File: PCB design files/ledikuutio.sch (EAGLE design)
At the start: 54 parts, among them IC1 ATMEGA328P, IC3 74HC595D, Q2 MOSFET-NCHANNELSMD, Q3 16mhz, T1 TIP42, T2 TIP42, T3 TIP42, T4 TIP42, T5 TIP42, T6 TIP42, T7 TIP42, T8 TIP42, X1 2516-, X2 5566-20, X3 2516-, X4 2516-, X5 2516-, X6 2510-

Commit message: Updated the designs...
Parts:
- added C18, C19: 100nF, rcl:C-EUC0603
- added IC2: ISO7221A, texas:ISO7221A
- added R11, R12, R13, R14, R15, R16, R17, R18: 1k, rcl:R-EU_M0805
- F1, F2: value (none) -> 2A; device fuse:GSH15 -> special:FUSE
- R10, R3, R4, R5, R6, R7, R8, R9: device rc-master:R_0805 -> rcl:R-EU_M0805
- R2: device resistor:R-US_R0805 -> rcl:R-EU_M0805
- U$1, U$2, U$3, U$4: value TLC5940TLC5940NT -> TLC5940TLC5940PWP; device elovalo:TLC5940TLC5940NT -> elovalo:TLC5940TLC5940PWP
- UART: device con-lsta:FE06-1 -> elovalo:FE06-1
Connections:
- removed net DCPRG: IC1.PD6(AIN0), U$1TLC5940.DCPRG, U$2TLC5940.DCPRG, U$3TLC5940.DCPRG, U$4TLC5940.DCPRG
- removed net VPRG: IC1.PD5(T1), U$1TLC5940.VPRG, U$2TLC5940.VPRG, U$3TLC5940.VPRG, U$4TLC5940.VPRG
- new net GND1: C18.2, IC2.GND1, UART.1
- new net RXD_FT232R: IC2.INB, UART.5
- new net TXD_FT232R: IC2.OUTA, UART.4
- new net VDD: C18.1, IC2.VCC1, UART.3
- net +5V: now also F2.2, IC3A.SCL; no longer F1.1
- net BLANK: now also IC1.PB2(SS/OC1B); no longer IC1.PD7(AIN1)
- net GND: now also C19.2, IC2.GND2, U$1TLC5940.DCPRG, U$1TLC5940.VPRG, U$1TLC5940_PWR.GND@1, U$2TLC5940.DCPRG, U$2TLC5940.VPRG, U$2TLC5940_PWR.GND@1, U$3TLC5940.DCPRG, U$3TLC5940.VPRG, U$3TLC5940_PWR.GND@1, U$4TLC5940.DCPRG, U$4TLC5940.VPRG, U$4TLC5940_PWR.GND@1; no longer U$1TLC5940_PWR.GND, U$2TLC5940_PWR.GND, U$3TLC5940_PWR.GND, U$4TLC5940_PWR.GND, UART.1
- net N$10: now also R18.2
- net N$11: now also R12.2
- net N$12: now also R13.2
- net N$13: now also R15.2
- net N$14: now also R17.2
- net N$23: now also R13.1
- net N$24: now also R12.1
- net N$25: now also R11.1
- net N$26: now also R14.1
- net N$27: now also R15.1
- net N$28: now also R16.1
- net N$29: now also R17.1
- net N$30: now also R18.1
- net N$48: now also F2.1; no longer F1.2
- net N$5: now also F1.1; no longer F2.2
- net N$7: now also R11.2
- net N$8: now also R14.2
- net N$9: now also R16.2
- net PS_ON: now also IC1.PD3(INT1); no longer IC1.PD4(XCK/T0)
- net RXD: now also IC2.OUTB; no longer UART.4
- net TXD: now also IC2.INA; no longer UART.5
- net VCC: now also C19.1, F1.2, IC2.VCC2; no longer F2.1, IC3A.SCL, UART.3
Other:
- note added: "Kysy joelilta oikea pinijärjestys..."
- note removed: "Power supply"
- moved on the sheet: C1, C10, C11, C12, C13, C14, C15, C16, C17, C2, C3, C4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

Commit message: Signal area in PCB almost ready.
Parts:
- removed F1, F2: 2A, special:FUSE
- added C20, C22: 10nF, rcl:C-EUC0805
- added C21, C23: 100nF, rcl:C-EUC0805
- added R19, R20: 10k, rcl:R-EU_M0805
- added S1: RESET, SparkFun:SWITCH-MOMENTARY-2SMD
- added X7: ANALOG IO, con-3m:2510-
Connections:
- removed net N$48: C17.+, F2.1, X2-19.S, X2-20.S, X2-4.S, X2-6.S
- removed net N$5: F1.1, X2-9.S
- new net ADC0: IC1.PC0(ADC0), X7-1.KL
- new net ADC1: IC1.PC1(ADC1), X7-2.KL
- new net ADC2: IC1.PC2(ADC2), X7-3.KL
- new net ADC3: IC1.PC3(ADC3), X7-4.KL
- new net ADC4: IC1.PC4(ADC4/SDA), X7-5.KL
- new net ADC5: IC1.PC5(ADC5/SCL), X7-6.KL
- new net ADC6: IC1.ADC6, X7-7.KL
- new net ADC7: IC1.ADC7, X7-8.KL
- net +5V: now also C17.+, X2-19.S, X2-20.S, X2-4.S, X2-6.S; no longer F2.2
- net GND: now also C20.2, C21.2, C22.2, C23.2, IC1.AGND, R19.2, S1.2, X7-10.KL
- net PS_ON: now also R19.1
- net RESET: now also R20.1, S1.1
- net VCC: now also C20.1, C21.1, C22.1, C23.1, IC1.AVCC, R20.2, X2-9.S, X7-9.KL; no longer F1.2
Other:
- note added: "AVCC decoupling"
- moved on the sheet: C1, C2, Q3

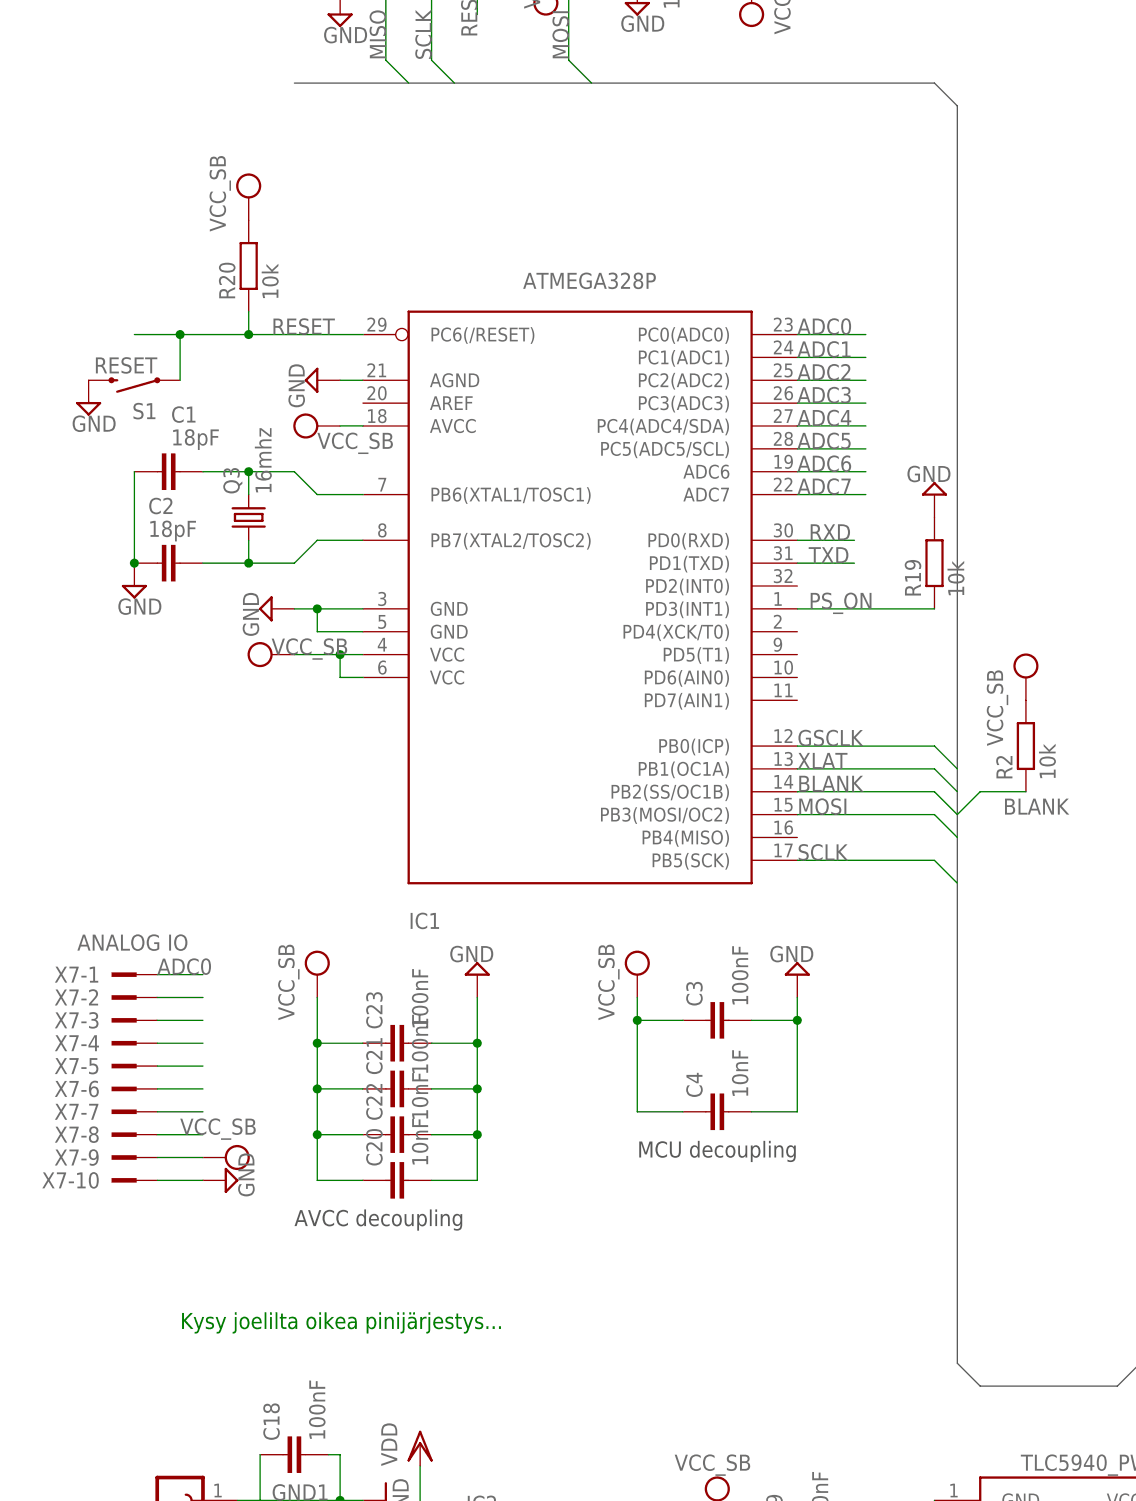
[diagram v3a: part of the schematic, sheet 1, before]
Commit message: Add up to date schematics.pdf and minor changes to the chematic and layout.
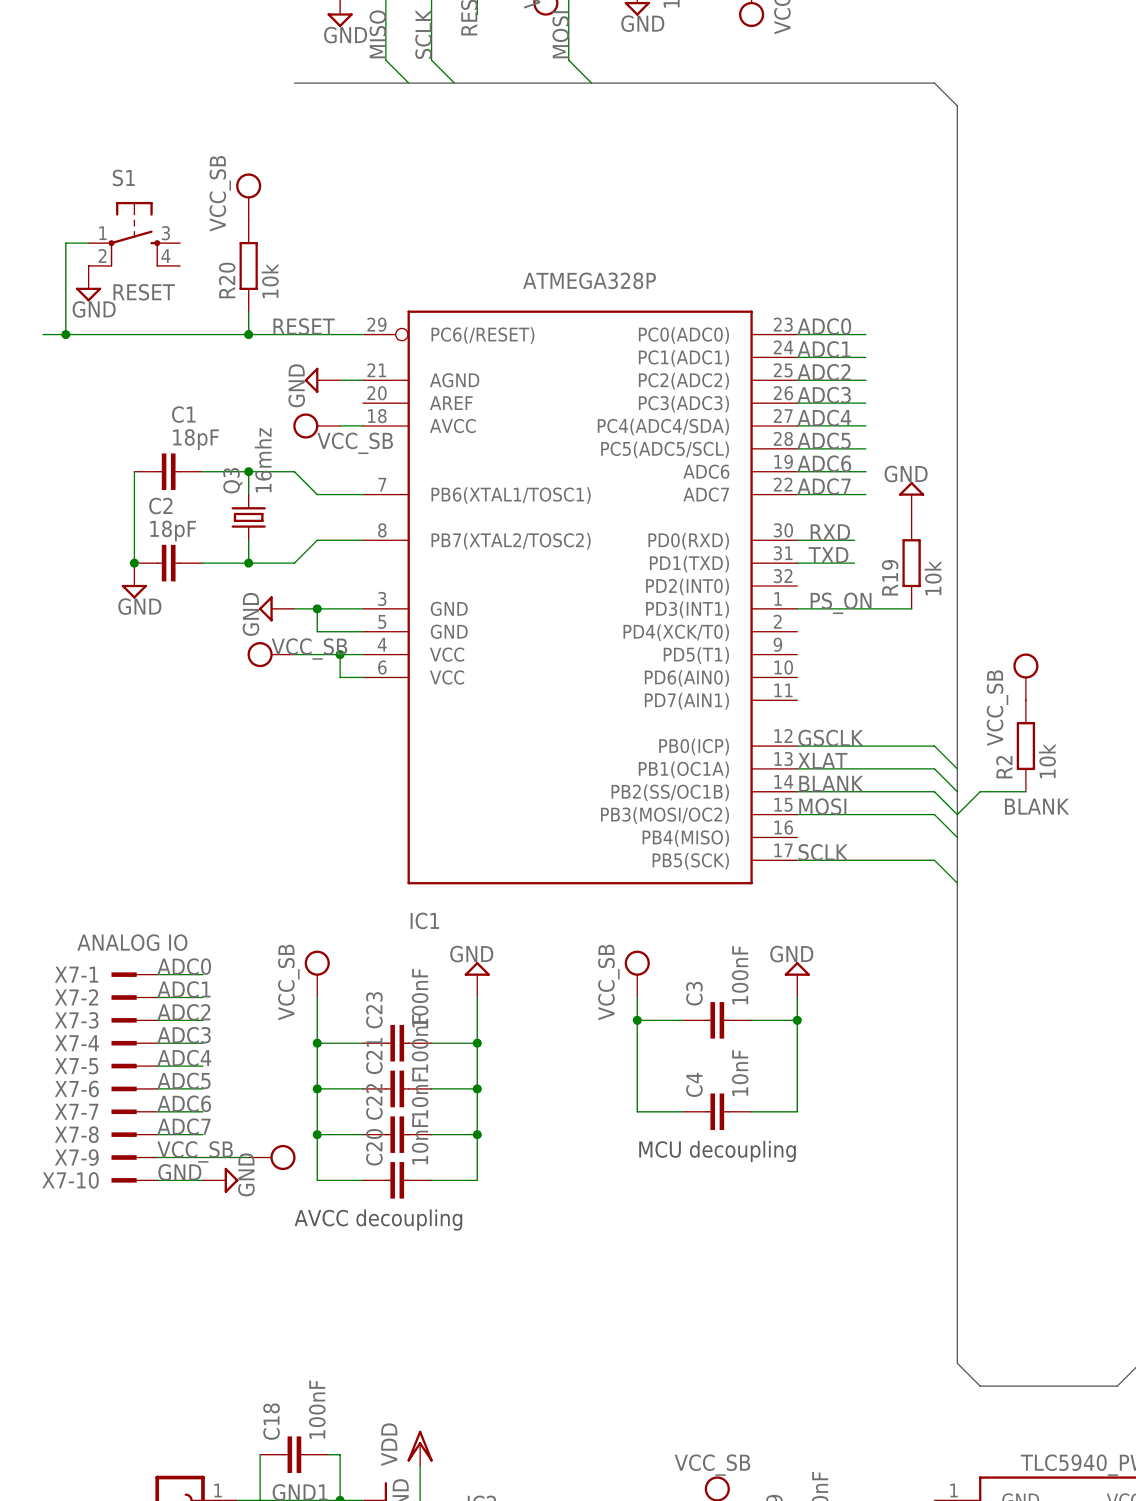
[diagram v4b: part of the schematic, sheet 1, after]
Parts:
- S1: device SparkFun:SWITCH-MOMENTARY-2SMD -> SparkFun:TAC_SWITCHSMD
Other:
- note removed: "Kysy joelilta oikea pinijärjestys..."
- moved on the sheet: R19
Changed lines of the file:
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@@
 <part name="C22" library="rcl" deviceset="C-EU" device="C0805" value="10nF"/>
 <part name="C23" library="rcl" deviceset="C-EU" device="C0805" value="100nF"/>
-<part name="S1" library="SparkFun" deviceset="SWITCH-MOMENTARY-2" device="SMD" value="RESET"/>
+<part name="S1" library="SparkFun" deviceset="TAC_SWITCH" device="SMD" value="RESET"/>
 <part name="VCC_SB12" library="supply2" deviceset="VCC" device="" value="VCC_SB"/>
 <part name="SUPPLY25" library="supply2" deviceset="GND" device=""/>
@@
 <text x="81.28" y="106.68" size="1.778" layer="97">MCU decoupling</text>
 <text x="327.66" y="233.68" size="1.778" layer="91">Clock Divider</text>
-<text x="30.48" y="87.63" size="1.778" layer="91">Kysy joelilta oikea pinijärjestys...</text>
 <text x="43.18" y="99.06" size="1.778" layer="97">AVCC decoupling</text>
 </plain>
@@
 <attribute name="VALUE" x="43.18" y="121.92" size="1.778" layer="96" rot="R90"/>
 </instance>
-<instance part="VCC_SB11" gate="G$1" x="35.56" y="106.68" smashed="yes" rot="R270">
-<attribute name="VALUE" x="30.48" y="109.22" size="1.778" layer="96"/>
+<instance part="VCC_SB11" gate="G$1" x="40.64" y="106.68" smashed="yes" rot="R270">
+<attribute name="VALUE" x="27.94" y="106.68" size="1.778" layer="96"/>
 </instance>
 <instance part="SUPPLY23" gate="GND" x="35.56" y="104.14" rot="R90"/>
-<instance part="R19" gate="G$1" x="114.3" y="172.72" rot="R90"/>
-<instance part="SUPPLY24" gate="GND" x="114.3" y="180.34" rot="R180"/>
+<instance part="R19" gate="G$1" x="111.76" y="172.72" rot="R90"/>
+<instance part="SUPPLY24" gate="GND" x="111.76" y="180.34" rot="R180"/>
 <instance part="C22" gate="G$1" x="53.34" y="109.22" rot="R90"/>
 <instance part="C23" gate="G$1" x="53.34" y="119.38" rot="R90"/>
-<instance part="S1" gate="G$1" x="25.4" y="193.04" rot="R180"/>
+<instance part="S1" gate="S" x="25.4" y="208.28"/>
 <instance part="VCC_SB12" gate="G$1" x="38.1" y="213.36" smashed="yes">
 <attribute name="VALUE" x="35.56" y="209.55" size="1.778" layer="96" rot="R90"/>
 </instance>
-<instance part="SUPPLY25" gate="GND" x="20.32" y="190.5"/>
+<instance part="SUPPLY25" gate="GND" x="20.32" y="203.2"/>
 <instance part="R20" gate="G$1" x="38.1" y="205.74" rot="R90"/>
 </instances>
@@
 <wire x1="27.94" y1="104.14" x2="33.02" y2="104.14" width="0.1524" layer="91"/>
 <pinref part="SUPPLY23" gate="GND" pin="GND"/>
+<label x="27.94" y="104.14" size="1.778" layer="95"/>
 </segment>
 <segment>
@@
 </segment>
 <segment>
-<pinref part="S1" gate="G$1" pin="2"/>
+<pinref part="S1" gate="S" pin="2"/>
 <pinref part="SUPPLY25" gate="GND" pin="GND"/>
 </segment>
@@
 <segment>
 <pinref part="X7" gate="-9" pin="KL"/>
-<wire x1="27.94" y1="106.68" x2="33.02" y2="106.68" width="0.1524" layer="91"/>
+<wire x1="27.94" y1="106.68" x2="38.1" y2="106.68" width="0.1524" layer="91"/>
 <pinref part="VCC_SB11" gate="G$1" pin="VCC"/>
 </segment>
@@
 <segment>
 <label x="40.64" y="198.12" size="1.778" layer="95"/>
-<pinref part="S1" gate="G$1" pin="1"/>
-<wire x1="38.1" y1="198.12" x2="30.48" y2="198.12" width="0.1524" layer="91"/>
-<wire x1="30.48" y1="198.12" x2="30.48" y2="193.04" width="0.1524" layer="91"/>
+<pinref part="S1" gate="S" pin="1"/>
+<wire x1="38.1" y1="198.12" x2="17.78" y2="198.12" width="0.1524" layer="91"/>
+<wire x1="17.78" y1="198.12" x2="17.78" y2="208.28" width="0.1524" layer="91"/>
+<wire x1="17.78" y1="208.28" x2="20.32" y2="208.28" width="0.1524" layer="91"/>
 <pinref part="R20" gate="G$1" pin="1"/>
 <wire x1="38.1" y1="200.66" x2="38.1" y2="198.12" width="0.1524" layer="91"/>
@@
 <wire x1="38.1" y1="198.12" x2="50.8" y2="198.12" width="0.1524" layer="91"/>
 <junction x="38.1" y="198.12"/>
-<wire x1="30.48" y1="198.12" x2="25.4" y2="198.12" width="0.1524" layer="91"/>
-<junction x="30.48" y="198.12"/>
+<wire x1="17.78" y1="198.12" x2="15.24" y2="198.12" width="0.1524" layer="91"/>
+<junction x="17.78" y="198.12"/>
 </segment>
 <segment>
@@
 <net name="PS_ON" class="1">
 <segment>
-<wire x1="99.06" y1="167.64" x2="114.3" y2="167.64" width="0.1524" layer="91"/>
+<wire x1="99.06" y1="167.64" x2="111.76" y2="167.64" width="0.1524" layer="91"/>
 <pinref part="IC1" gate="G$1" pin="PD3(INT1)"/>
 <label x="100.33" y="167.64" size="1.778" layer="95"/>
@@
 <wire x1="33.02" y1="124.46" x2="27.94" y2="124.46" width="0.1524" layer="91"/>
 <label x="99.06" y="195.58" size="1.778" layer="95"/>
+<label x="27.94" y="124.46" size="1.778" layer="95"/>
 </segment>
 </net>
@@
 <pinref part="X7" gate="-3" pin="KL"/>
 <label x="99.06" y="193.04" size="1.778" layer="95"/>
+<label x="27.94" y="121.92" size="1.778" layer="95"/>
 </segment>
 </net>
@@
 <pinref part="X7" gate="-4" pin="KL"/>
 <wire x1="27.94" y1="119.38" x2="33.02" y2="119.38" width="0.1524" layer="91"/>
+<label x="27.94" y="119.38" size="1.778" layer="95"/>
 </segment>
 </net>
@@
 <pinref part="X7" gate="-5" pin="KL"/>
 <wire x1="27.94" y1="116.84" x2="33.02" y2="116.84" width="0.1524" layer="91"/>
+<label x="27.94" y="116.84" size="1.778" layer="95"/>
 </segment>
 </net>
@@
 <pinref part="X7" gate="-6" pin="KL"/>
 <wire x1="27.94" y1="114.3" x2="33.02" y2="114.3" width="0.1524" layer="91"/>
+<label x="27.94" y="114.3" size="1.778" layer="95"/>
 </segment>
 </net>
@@
 <pinref part="X7" gate="-7" pin="KL"/>
 <wire x1="27.94" y1="111.76" x2="33.02" y2="111.76" width="0.1524" layer="91"/>
+<label x="27.94" y="111.76" size="1.778" layer="95"/>
 </segment>
 </net>
@@
 <pinref part="X7" gate="-8" pin="KL"/>
 <wire x1="27.94" y1="109.22" x2="33.02" y2="109.22" width="0.1524" layer="91"/>
-</segment>
-</net>
+<label x="27.94" y="109.22" size="1.778" layer="95"/>
+</segment>
+</net>

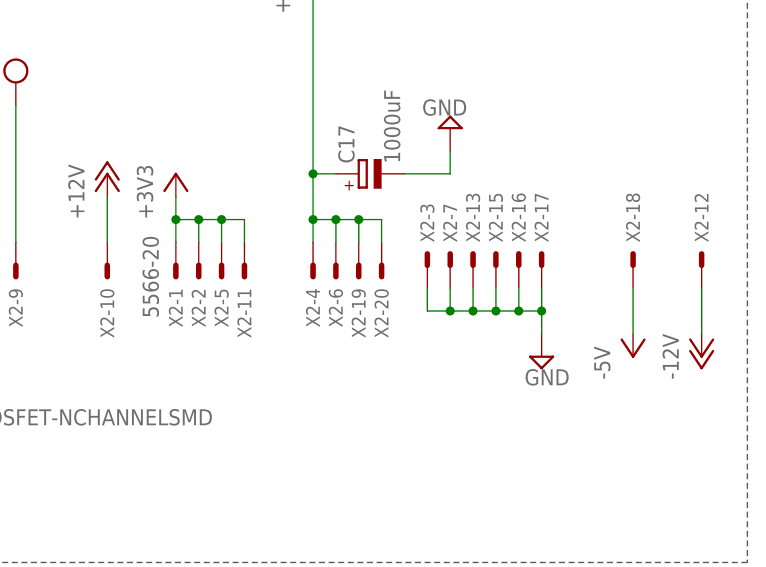
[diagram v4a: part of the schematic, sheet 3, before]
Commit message: Fix schematic. 3.3V rail was connected to GND.
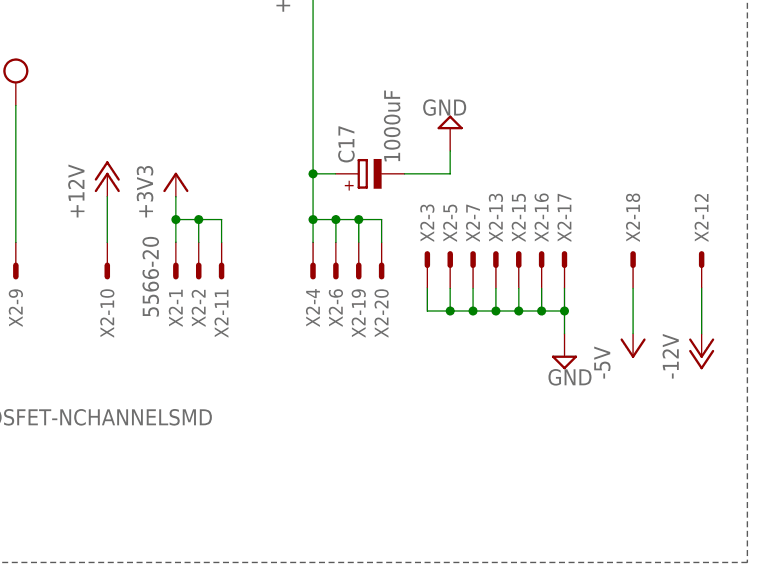
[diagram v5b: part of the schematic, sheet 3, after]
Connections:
- net +3V3: no longer X2-5.S
- net GND: now also X2-5.S
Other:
- moved on the sheet: X2-11, X2-13, X2-15, X2-16, X2-17, X2-5, X2-7
